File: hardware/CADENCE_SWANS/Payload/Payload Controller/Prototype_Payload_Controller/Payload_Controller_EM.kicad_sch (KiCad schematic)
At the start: 0 parts

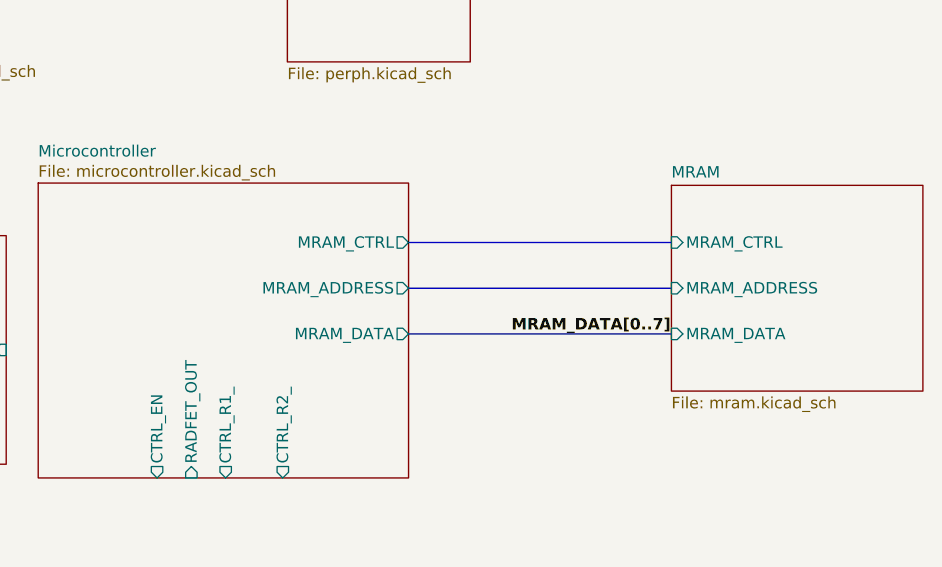
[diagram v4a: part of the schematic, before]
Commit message: resolved bus naming issues
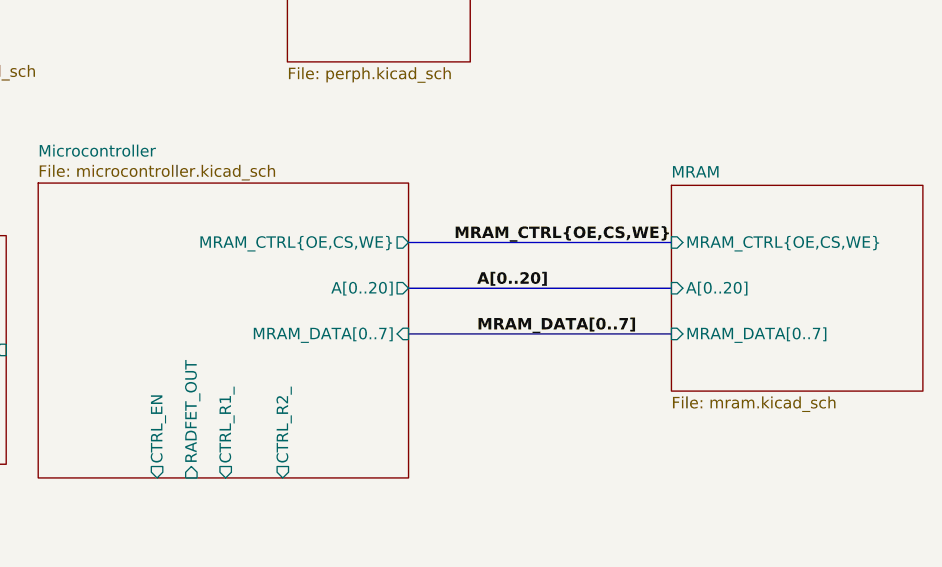
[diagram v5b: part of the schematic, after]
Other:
- sheet MRAM ports: added A[0..20], MRAM_CTRL{OE,CS,WE}, MRAM_DATA[0..7]; removed MRAM_ADDRESS, MRAM_CTRL, MRAM_DATA
- sheet Microcontroller ports: added A[0..20], MRAM_CTRL{OE,CS,WE}, MRAM_DATA[0..7]; removed MRAM_ADDRESS, MRAM_CTRL, MRAM_DATA
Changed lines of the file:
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@@
 	(bus
 		(pts
+			(xy 142.24 198.12) (xy 143.51 198.12)
+		)
+		(stroke
+			(width 0)
+			(type default)
+		)
+	)
+	(wire
+		(pts
+			(xy 107.95 82.55) (xy 113.03 82.55)
+		)
+		(stroke
+			(width 0)
+			(type default)
+		)
+	)
+	(bus
+		(pts
+			(xy 224.79 82.55) (xy 254 82.55)
+		)
+		(stroke
+			(width 0)
+			(type default)
+		)
+	)
+	(bus
+		(pts
 			(xy 224.79 87.63) (xy 254 87.63)
 		)
@@
 		)
 	)
-	(bus
-		(pts
-			(xy 142.24 198.12) (xy 143.51 198.12)
-		)
-		(stroke
-			(width 0)
-			(type default)
-		)
-	)
 	(wire
 		(pts
-			(xy 107.95 82.55) (xy 113.03 82.55)
-		)
-		(stroke
-			(width 0)
-			(type default)
-		)
-	)
-	(bus
-		(pts
-			(xy 224.79 82.55) (xy 254 82.55)
-		)
-		(stroke
-			(width 0)
-			(type default)
-		)
-	)
-	(wire
-		(pts
 			(xy 60.96 86.36) (xy 77.47 86.36)
 		)
@@
 	)
 	(label "MRAM_DATA[0..7]"
-		(at 236.22 87.63 0)
+		(at 232.41 87.63 0)
+		(effects
+			(font
+				(size 1.27 1.27)
+				(thickness 0.254)
+				(bold yes)
+			)
+			(justify left bottom)
+		)
+	)
+	(label "MRAM_CTRL{OE,CS,WE}"
+		(at 229.87 77.47 0)
+		(effects
+			(font
+				(size 1.27 1.27)
+				(thickness 0.254)
+				(bold yes)
+			)
+			(justify left bottom)
+		)
+	)
+	(label "A[0..20]"
+		(at 232.41 82.55 0)
 		(effects
 			(font
@@
 			)
 		)
-		(pin "MRAM_CTRL" output
+		(pin "MRAM_CTRL{OE,CS,WE}" output
 			(at 224.79 77.47 0)
 			(effects
@@
 			)
 		)
-		(pin "MRAM_DATA" output
+		(pin "A[0..20]" output
+			(at 224.79 82.55 0)
+			(effects
+				(font
+					(size 1.27 1.27)
+				)
+				(justify right)
+			)
+		)
+		(pin "MRAM_DATA[0..7]" input
 			(at 224.79 87.63 0)
-			(effects
-				(font
-					(size 1.27 1.27)
-				)
-				(justify right)
-			)
-		)
-		(pin "MRAM_ADDRESS" output
-			(at 224.79 82.55 0)
 			(effects
 				(font
@@
 			)
 		)
-		(pin "MRAM_ADDRESS" input
+		(pin "A[0..20]" input
 			(at 254 82.55 180)
 			(effects
@@
 			)
 		)
-		(pin "MRAM_CTRL" input
+		(pin "MRAM_CTRL{OE,CS,WE}" input
 			(at 254 77.47 180)
 			(effects
@@
 			)
 		)
-		(pin "MRAM_DATA" input
+		(pin "MRAM_DATA[0..7]" input
 			(at 254 87.63 180)
 			(effects

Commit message: clean up
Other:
- sheet Debug ports: added none; removed UART
- sheet Flight Computer Interface ports: added Payload_Rx, Payload_Tx; removed UART
- sheet Instrument ports: added CTRL_EN_[0..4], CTRL_R1_[0..4], CTRL_R2_[0..4], RADFET_OUT[0..4]; removed CTRL_EN_, CTRL_R1_, CTRL_R2_, RADFET_OUT
- sheet Microcontroller ports: added CTRL_EN_[0..4], CTRL_R1_[0..4], CTRL_R2_[0..4], I2C0_SCL, I2C0_SDA, Payload_Rx, Payload_Tx, RADFET_OUT[0..4]; removed CTRL_EN, CTRL_R1_, CTRL_R2_, RADFET_OUT
- sheet Peripherals ports: added I2C0_SCL, I2C0_SDA; removed none

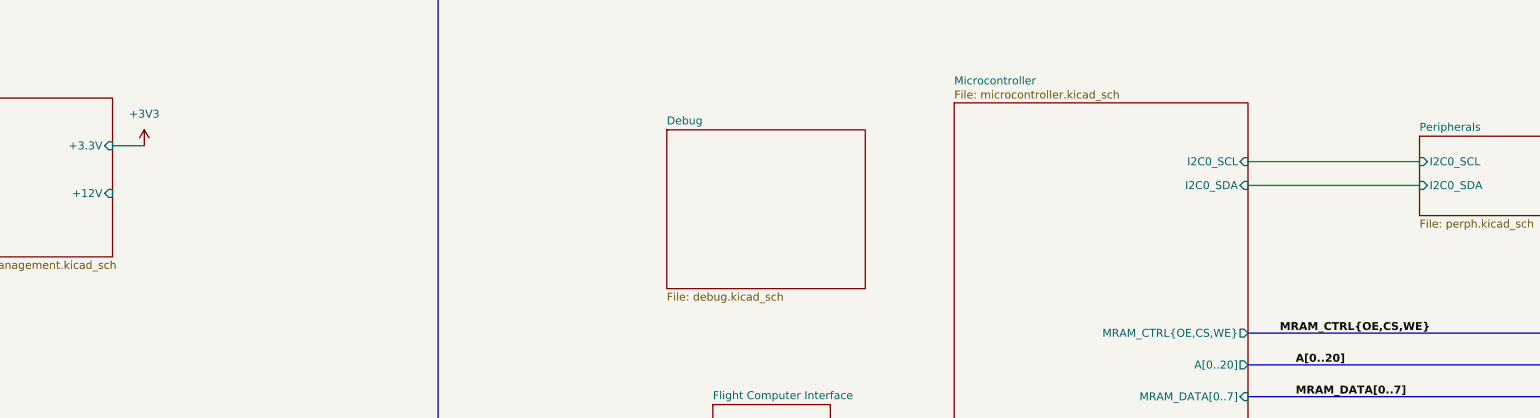
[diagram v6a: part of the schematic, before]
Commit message: identified debug and usb pins
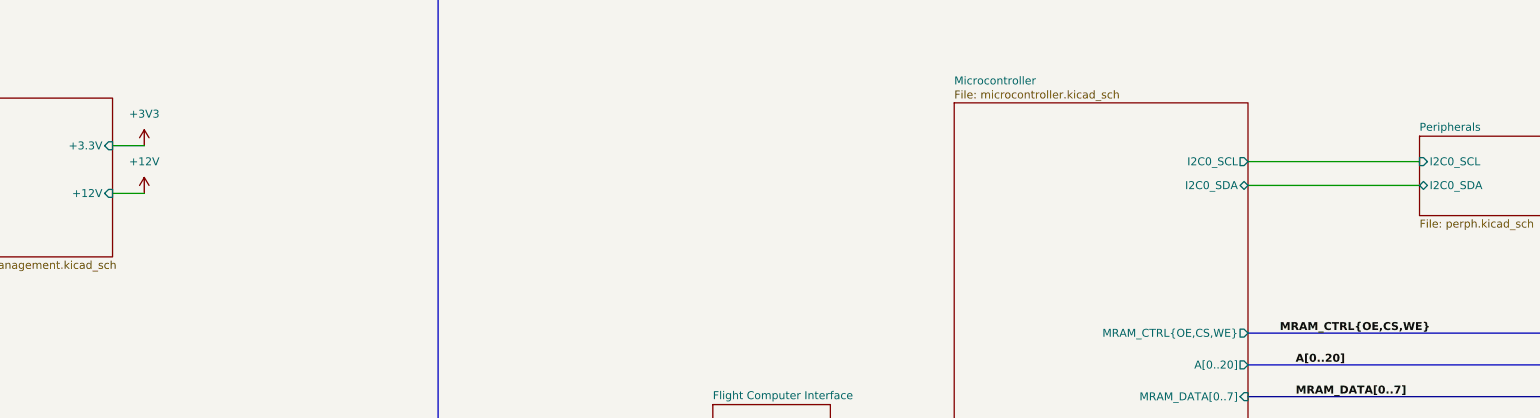
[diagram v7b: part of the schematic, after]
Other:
- removed sheet Debug
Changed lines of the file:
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@@
+		)
+	)
+	(wire
+		(pts
+			(xy 107.95 90.17) (xy 113.03 90.17)
+		)
+		(stroke
+			(width 0)
+			(type default)
 		)
 	)
@@
 	)
 	(symbol
+		(lib_id "power:+12V")
+		(at 113.03 90.17 0)
+		(unit 1)
+		(exclude_from_sim no)
+		(in_bom yes)
+		(on_board yes)
+		(dnp no)
+		(fields_autoplaced yes)
+		(property "Reference" "#PWR090"
+			(at 113.03 93.98 0)
+			(effects
+				(font
+					(size 1.27 1.27)
+				)
+				(hide yes)
+			)
+		)
+		(property "Value" "+12V"
+			(at 113.03 85.09 0)
+			(effects
+				(font
+					(size 1.27 1.27)
+				)
+			)
+		)
+		(property "Footprint" ""
+			(at 113.03 90.17 0)
+			(effects
+				(font
+					(size 1.27 1.27)
+				)
+				(hide yes)
+			)
+		)
+		(property "Datasheet" ""
+			(at 113.03 90.17 0)
+			(effects
+				(font
+					(size 1.27 1.27)
+				)
+				(hide yes)
+			)
+		)
+		(property "Description" "Power symbol creates a global label with name \"+12V\""
+			(at 113.03 90.17 0)
+			(effects
+				(font
+					(size 1.27 1.27)
+				)
+				(hide yes)
+			)
+		)
+		(pin "1"
+		)
+		(instances
+			(project ""
+				(path "/866a965d-c307-40b7-9977-69e77fc0dc82"
+					(reference "#PWR090")
+					(unit 1)
+				)
+			)
+		)
+	)
+	(symbol
 		(lib_id "power:+3V3")
 		(at 113.03 82.55 0)
@@
 	)
 	(sheet
-		(at 196.596 80.01)
-		(size 31.75 25.4)
-		(exclude_from_sim no)
-		(in_bom yes)
-		(on_board yes)
-		(dnp no)
-		(fields_autoplaced yes)
+		(at 242.57 75.692)
+		(size 46.99 82.55)
+		(exclude_from_sim no)
+		(in_bom yes)
+		(on_board yes)
+		(dnp no)
 		(stroke
 			(width 0.1524)
@@
 		)
 		(fill
-			(color 0 0 0 0.0000)
-		)
-		(property "Sheetname" "Debug"
-			(at 196.596 79.2984 0)
-			(effects
-				(font
-					(size 1.27 1.27)
-				)
-				(justify left bottom)
-			)
-		)
-		(property "Sheetfile" "debug.kicad_sch"
-			(at 196.596 105.9946 0)
-			(effects
-				(font
-					(size 1.27 1.27)
-				)
-				(justify left top)
-			)
-		)
-		(instances
-			(project "Payload_Controller_EM"
-				(path "/866a965d-c307-40b7-9977-69e77fc0dc82"
-					(page "8")
-				)
-			)
-		)
-	)
-	(sheet
-		(at 242.57 75.692)
-		(size 46.99 82.55)
-		(exclude_from_sim no)
-		(in_bom yes)
-		(on_board yes)
-		(dnp no)
-		(stroke
-			(width 0.1524)
-			(type solid)
-		)
-		(fill
 			(color 220 249 255 1.0000)
 		)
@@
 			)
 		)
-		(pin "I2C0_SCL" input
+		(pin "I2C0_SCL" output
 			(at 289.56 85.09 0)
 			(effects
@@
 			)
 		)
-		(pin "I2C0_SDA" input
+		(pin "I2C0_SDA" bidirectional
 			(at 289.56 88.9 0)
 			(effects
@@
 			)
 		)
-		(pin "I2C0_SDA" input
+		(pin "I2C0_SDA" bidirectional
 			(at 316.992 88.9 180)
 			(effects

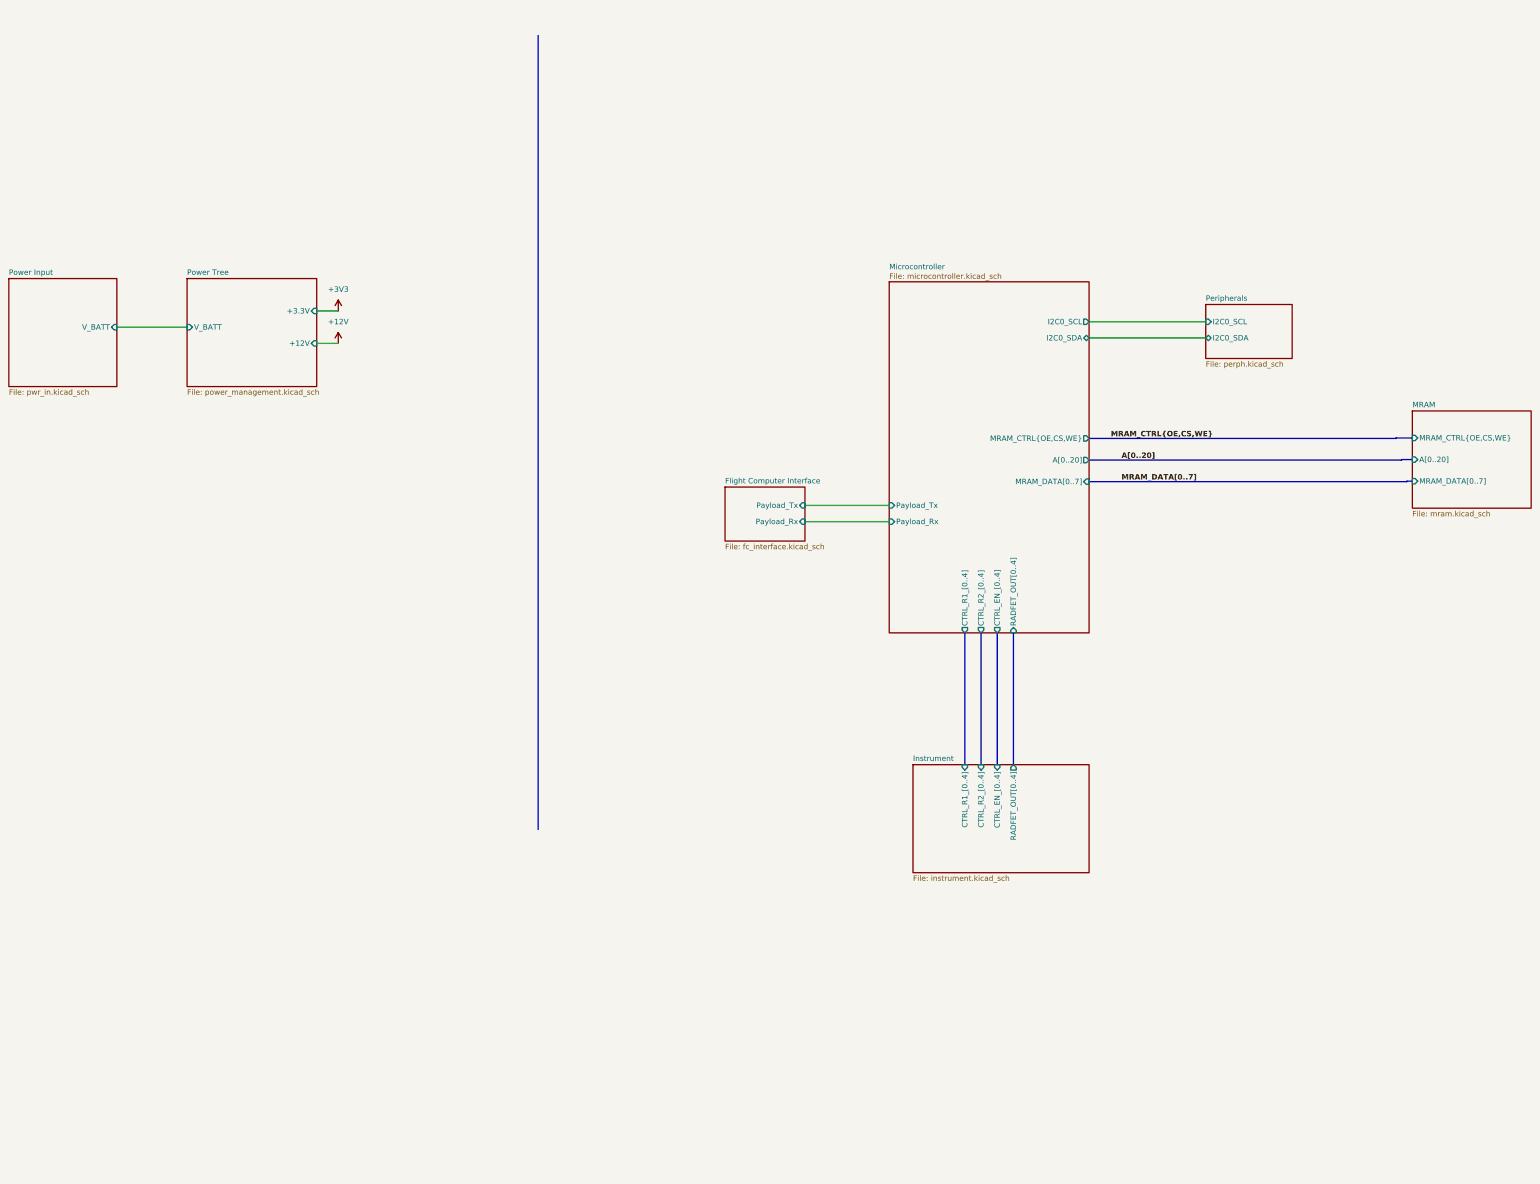
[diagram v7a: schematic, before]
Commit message: cleaned up schematics and assigned footprints for resistors and capacitors
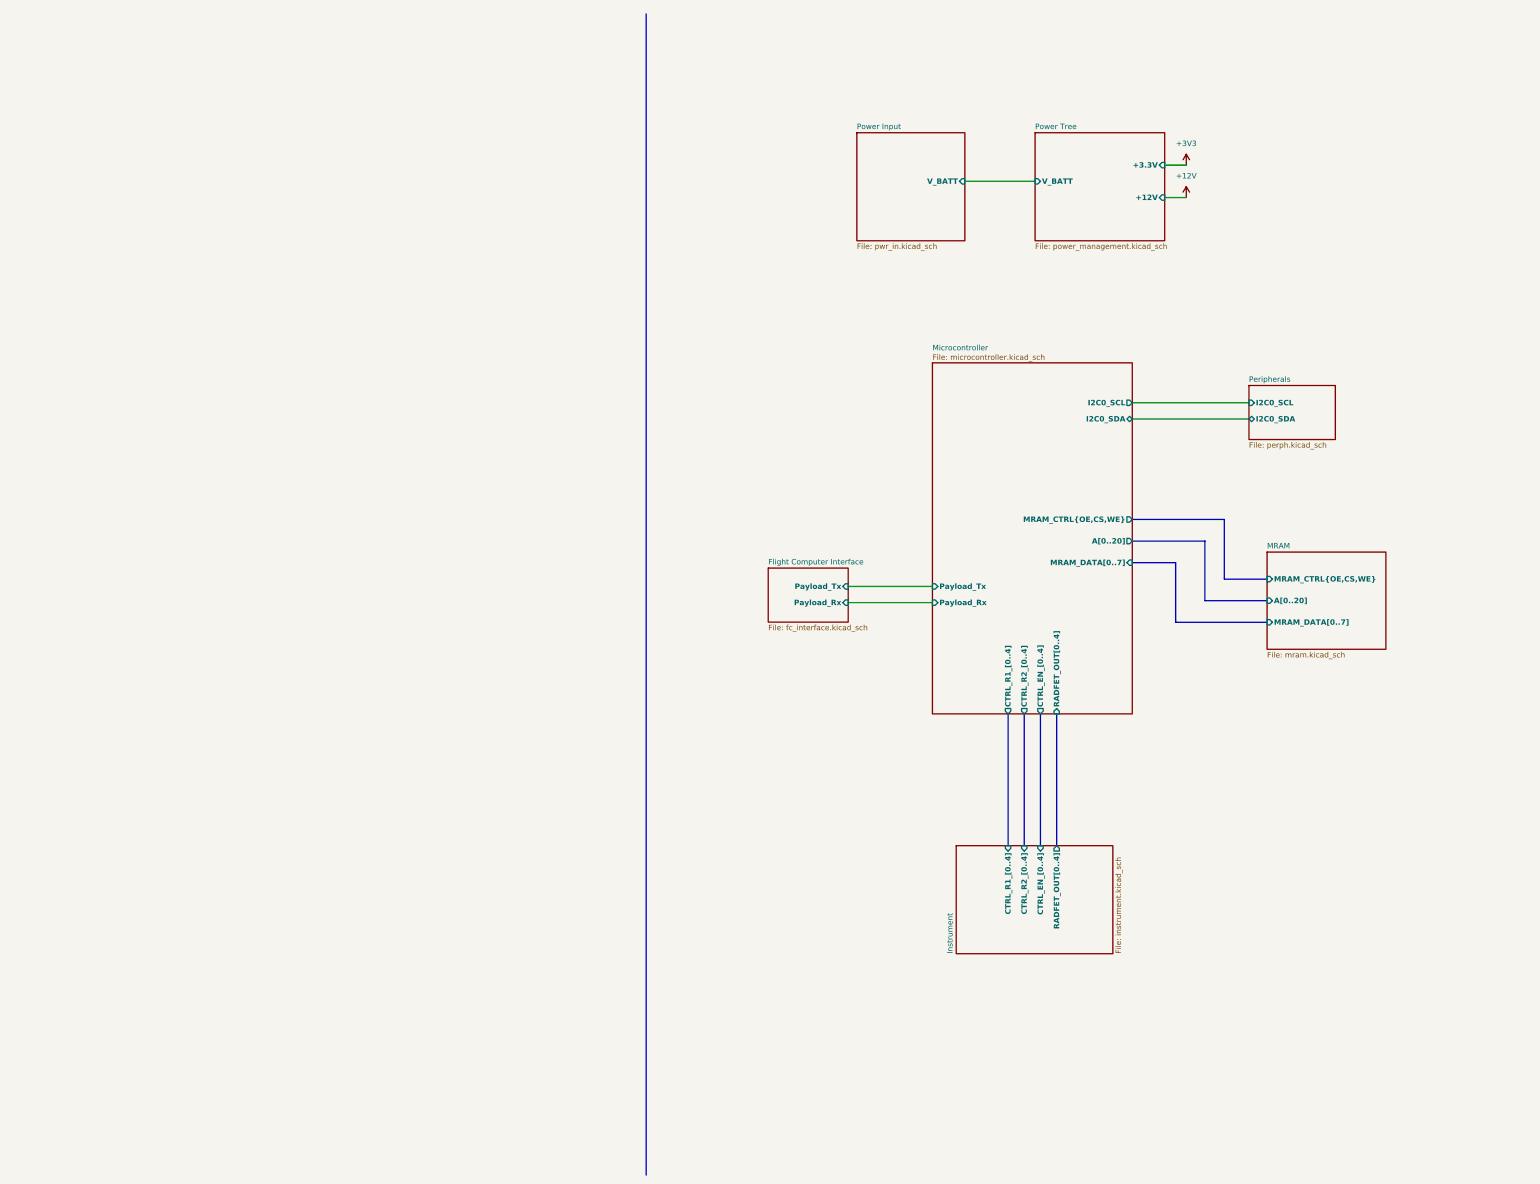
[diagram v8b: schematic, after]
